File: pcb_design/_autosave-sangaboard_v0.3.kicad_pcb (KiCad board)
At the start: 2 copper layers, 65 x 55 mm, 62 parts, among them J1 USB_Supply, J10 ISP, J11 USB_OTG, J12 X_AXIS, J13 Y_AXIS, J14 Z_AXIS, J2 USB_POWER OUT, J3 END_STOPS, J4 I2C Header, J5 Serial1 Header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

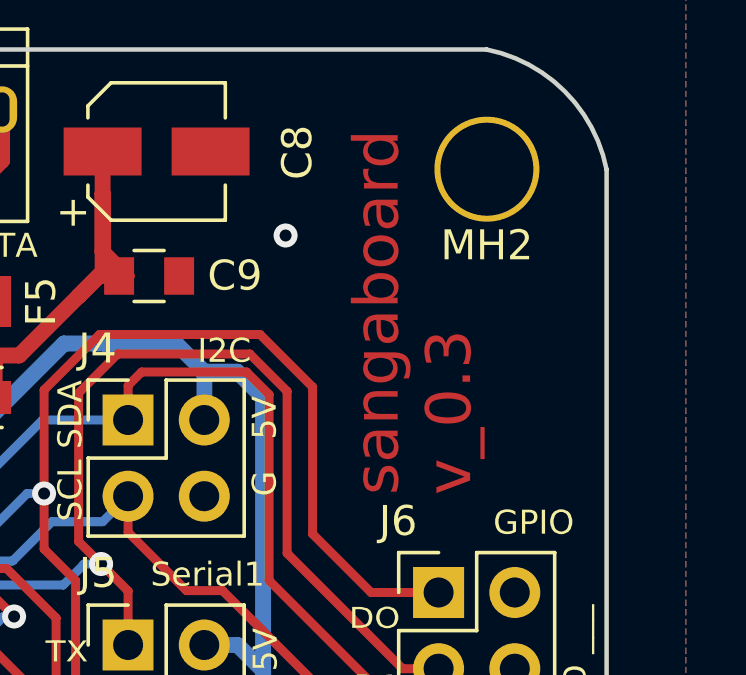
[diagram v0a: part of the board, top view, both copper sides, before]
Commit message: Remove diode between usb power in and out
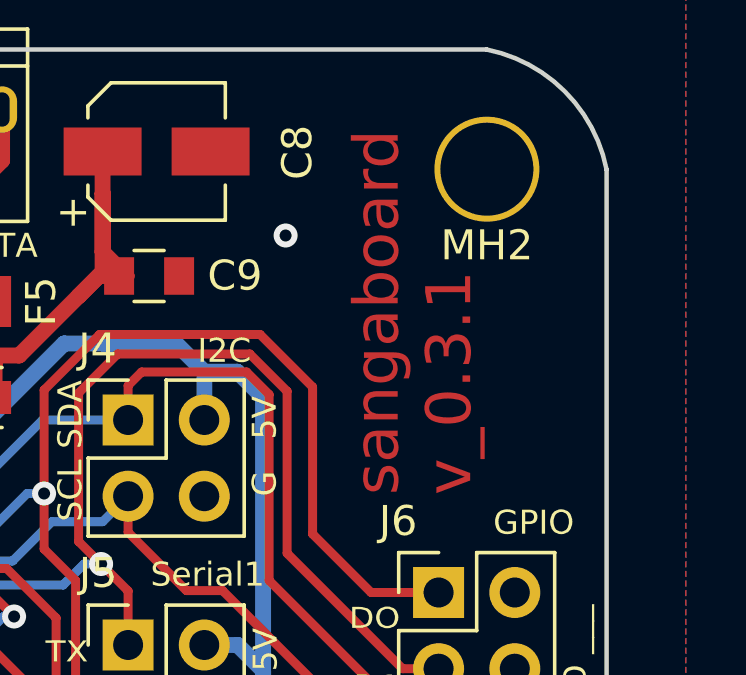
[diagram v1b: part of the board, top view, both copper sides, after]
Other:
- board text added: "sangaboard v_0.3.1"
- board text removed: "sangaboard v_0.3"
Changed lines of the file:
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@@
       (drillshape 0)
       (scaleselection 1)
-      (outputdirectory "sangaboard_V3_gerbers/"))
+      (outputdirectory "gerbers/"))
   )
   (net 0 "")
@@
     (effects (font (size 1.5 1.5) (thickness 0.3)) (justify mirror))
   )
-  (gr_text "sangaboard\nv_0.3" (at 158.55 59.85 90) (layer F.Cu)
+  (gr_text "sangaboard\nv_0.3.1" (at 158.55 59.85 90) (layer F.Cu)
     (effects (font (size 1.5 1.5) (thickness 0.25)) (justify left))
   )
@@
   (segment (start 124.1 63.9) (end 123.95 63.75) (width 0.3) (layer F.Cu) (net 4))
   (segment (start 126.4 63.9) (end 124.1 63.9) (width 0.3) (layer F.Cu) (net 4))
-  (segment (start 110.69 72.15) (end 110.35 71.81) (width 1.06) (layer F.Cu) (net 9))
-  (segment (start 112.3 72.15) (end 110.69 72.15) (width 1.06) (layer F.Cu) (net 9))
-  (segment (start 112.3 75.65) (end 112.3 72.15) (width 1.06) (layer F.Cu) (net 9))
-  (segment (start 110.35 67.31) (end 110.35 68.85) (width 1.06) (layer F.Cu) (net 9))
-  (segment (start 110.8 66.86) (end 110.35 67.31) (width 1.06) (layer F.Cu) (net 9))
-  (segment (start 110.8 64.95) (end 110.8 66.86) (width 1.06) (layer F.Cu) (net 9))
-  (segment (start 110.35 71.81) (end 110.35 68.85) (width 1.06) (layer F.Cu) (net 9))
   (segment (start 125.3 57.944998) (end 125.3 56.75) (width 0.3) (layer F.Cu) (net 5))
   (segment (start 127.655002 60.3) (end 127.655002 60.305002) (width 0.3) (layer F.Cu) (net 5))
@@
   (segment (start 117.92 78.95) (end 119.05 78.95) (width 0.53) (layer F.Cu) (net 8))
   (segment (start 119.05 78.95) (end 121.15 78.95) (width 0.53) (layer F.Cu) (net 8))
+  (segment (start 110.69 72.15) (end 110.35 71.81) (width 1.06) (layer F.Cu) (net 9))
+  (segment (start 112.3 72.15) (end 110.69 72.15) (width 1.06) (layer F.Cu) (net 9))
+  (segment (start 112.3 75.65) (end 112.3 72.15) (width 1.06) (layer F.Cu) (net 9))
+  (segment (start 110.35 67.31) (end 110.35 68.85) (width 1.06) (layer F.Cu) (net 9))
+  (segment (start 110.8 66.86) (end 110.35 67.31) (width 1.06) (layer F.Cu) (net 9))
+  (segment (start 110.8 64.95) (end 110.8 66.86) (width 1.06) (layer F.Cu) (net 9))
+  (segment (start 110.35 71.81) (end 110.35 68.85) (width 1.06) (layer F.Cu) (net 9))
   (segment (start 105.54 91.66) (end 103.12 91.66) (width 1.06) (layer F.Cu) (net 9))
   (segment (start 103.12 91.66) (end 101.56 90.1) (width 1.06) (layer F.Cu) (net 9))
